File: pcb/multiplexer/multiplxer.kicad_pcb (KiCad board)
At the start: 2 copper layers, 12 parts, among them J1 Conn_01x04, U1 74HC595, U2 4051

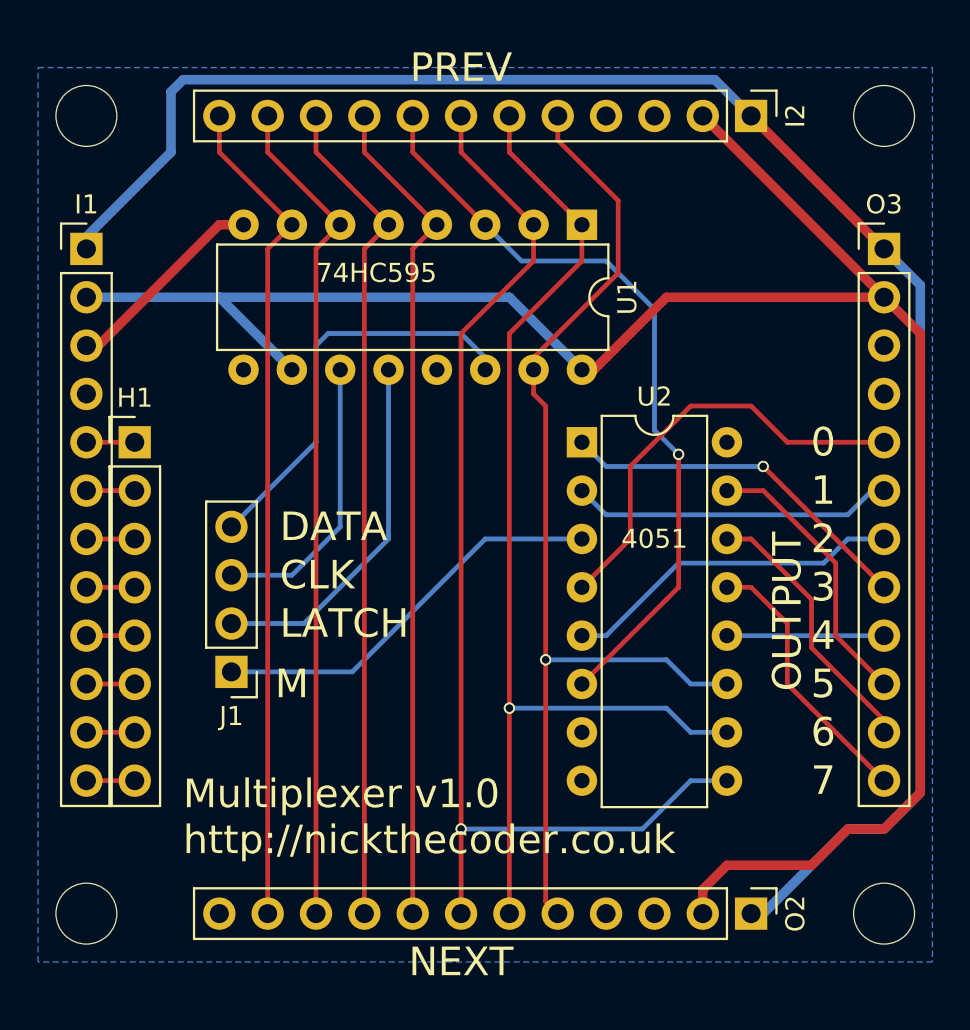
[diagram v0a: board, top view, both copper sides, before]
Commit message: Added terminal connectors to the header pins half module. Tweaked the MAX7219 module, and added both common anode and common cathode to stripLED modules.
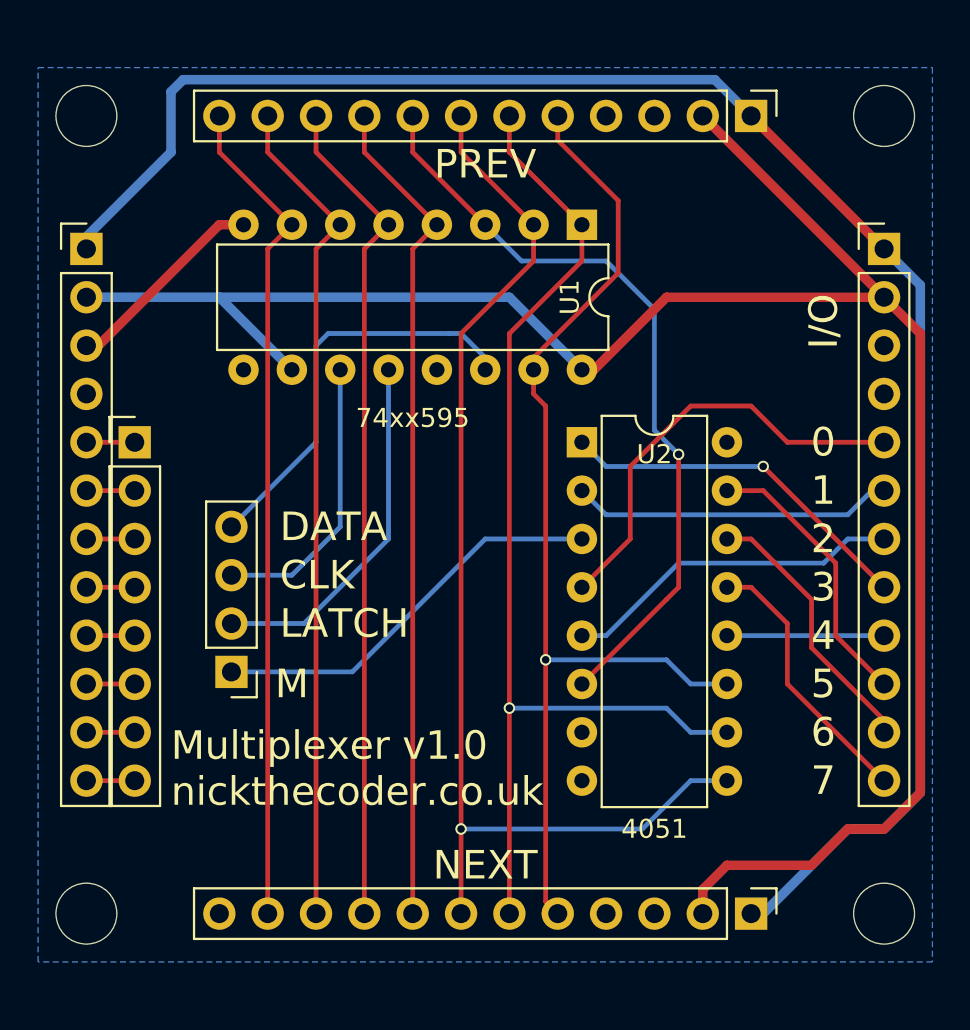
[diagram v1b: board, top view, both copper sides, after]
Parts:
- U1: value 74HC595 -> 74xx595
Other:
- board text added: "I/O"
- board text added: "Multiplexer v1.0 nickthecoder.co.uk"
- board text removed: "Multiplexer v1.0 http://nickthecoder.co.uk"
- board text removed: "OUTPUT"
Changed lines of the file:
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@@
     (links 52)
     (no_connects 0)
-    (area 124.46 82.55 173.990001 132.16)
+    (area 124.46 82.55 173.990001 132.080001)
     (thickness 1.6)
     (drawings 16)
@@
     (descr "Through hole straight pin header, 1x12, 2.54mm pitch, single row")
     (tags "Through hole pin header THT 1x12 2.54mm single row")
-    (fp_text reference I1 (at 0 -2.33) (layer F.SilkS)
+    (fp_text reference I1 (at 0 -2.33) (layer F.Fab)
       (effects (font (size 1 1) (thickness 0.15)))
     )
@@
     (descr "Through hole straight pin header, 1x08, 2.54mm pitch, single row")
     (tags "Through hole pin header THT 1x08 2.54mm single row")
-    (fp_text reference H1 (at 0 -2.33) (layer F.SilkS)
+    (fp_text reference H1 (at 0 -2.33) (layer F.Fab)
       (effects (font (size 1 1) (thickness 0.15)))
     )
@@
     (descr "Through hole straight pin header, 1x12, 2.54mm pitch, single row")
     (tags "Through hole pin header THT 1x12 2.54mm single row")
-    (fp_text reference I2 (at 0 -2.33 270) (layer F.SilkS)
+    (fp_text reference I2 (at 0 -2.33 270) (layer F.Fab)
       (effects (font (size 1 1) (thickness 0.15)))
     )
@@
     (descr "Through hole straight socket strip, 1x12, 2.54mm pitch, single row")
     (tags "Through hole socket strip THT 1x12 2.54mm single row")
-    (fp_text reference O2 (at 0 -2.33 270) (layer F.SilkS)
+    (fp_text reference O2 (at 0 -2.33 270) (layer F.Fab)
       (effects (font (size 1 1) (thickness 0.15)))
     )
@@
     (fp_line (start 1.8 29.75) (end 1.8 -1.8) (layer F.CrtYd) (width 0.05))
     (fp_line (start 1.8 -1.8) (end -1.8 -1.8) (layer F.CrtYd) (width 0.05))
-    (fp_text user %R (at 0 -2.33 270) (layer F.Fab)
+    (fp_text user %R (at 0 -2.33 270) (layer F.Fab) hide
       (effects (font (size 1 1) (thickness 0.15)))
     )
@@
     (descr "Through hole straight socket strip, 1x12, 2.54mm pitch, single row")
     (tags "Through hole socket strip THT 1x12 2.54mm single row")
-    (fp_text reference O3 (at 0 -2.33) (layer F.SilkS)
+    (fp_text reference O3 (at 0 -2.33) (layer F.Fab)
       (effects (font (size 1 1) (thickness 0.15)))
     )
@@
     (fp_line (start 1.8 29.75) (end 1.8 -1.8) (layer F.CrtYd) (width 0.05))
     (fp_line (start 1.8 -1.8) (end -1.8 -1.8) (layer F.CrtYd) (width 0.05))
-    (fp_text user %R (at 0 -2.33) (layer F.Fab)
+    (fp_text user %R (at 0 -2.33) (layer F.Fab) hide
       (effects (font (size 1 1) (thickness 0.15)))
     )
@@
     (descr "16-lead dip package, row spacing 7.62 mm (300 mils)")
     (tags "DIL DIP PDIP 2.54mm 7.62mm 300mil")
-    (fp_text reference U1 (at 3.81 -2.39 270) (layer F.SilkS)
-      (effects (font (size 1 1) (thickness 0.15)))
-    )
-    (fp_text value 74HC595 (at 2.54 10.795 360) (layer F.SilkS)
+    (fp_text reference U1 (at 3.81 0.635 270) (layer F.SilkS)
+      (effects (font (size 1 1) (thickness 0.15)))
+    )
+    (fp_text value 74xx595 (at 10.16 8.89 360) (layer F.SilkS)
       (effects (font (size 1 1) (thickness 0.15)))
     )
@@
     (descr "16-lead dip package, row spacing 7.62 mm (300 mils)")
     (tags "DIL DIP PDIP 2.54mm 7.62mm 300mil")
-    (fp_text reference U2 (at 3.81 -2.39) (layer F.SilkS)
-      (effects (font (size 1 1) (thickness 0.15)))
-    )
-    (fp_text value 4051 (at 3.81 5.08) (layer F.SilkS)
+    (fp_text reference U2 (at 3.81 0.635) (layer F.SilkS)
+      (effects (font (size 1 1) (thickness 0.15)))
+    )
+    (fp_text value 4051 (at 3.81 20.32) (layer F.SilkS)
       (effects (font (size 1 1) (thickness 0.15)))
     )
@@
     (descr "Through hole straight pin header, 1x04, 2.54mm pitch, single row")
     (tags "Through hole pin header THT 1x04 2.54mm single row")
-    (fp_text reference J1 (at 0 -2.33 180) (layer F.SilkS)
+    (fp_text reference J1 (at 0 -2.33 180) (layer F.Fab)
       (effects (font (size 1 1) (thickness 0.15)))
     )
@@
     (effects (font (size 1.5 1.5) (thickness 0.3)) (justify right))
   )
-  (gr_text PREV (at 147.955 83.82) (layer F.SilkS)
+  (gr_text PREV (at 149.225 88.9) (layer F.SilkS)
     (effects (font (size 1.5 1.5) (thickness 0.3)))
   )
-  (gr_text NEXT (at 147.955 130.81) (layer F.SilkS)
+  (gr_text NEXT (at 149.225 125.73) (layer F.SilkS)
     (effects (font (size 1.5 1.5) (thickness 0.3)))
   )
-  (gr_text OUTPUT (at 165.1 112.395 90) (layer F.SilkS)
+  (gr_text I/O (at 167.005 97.155 90) (layer F.SilkS)
     (effects (font (size 1.5 1.5) (thickness 0.3)))
   )
@@
     (effects (font (size 1.5 1.5) (thickness 0.3)) (justify left))
   )
-  (gr_text "Multiplexer v1.0\nhttp://nickthecoder.co.uk" (at 133.35 123.19) (layer F.SilkS)
+  (gr_text "Multiplexer v1.0\nnickthecoder.co.uk" (at 132.715 120.65) (layer F.SilkS)
     (effects (font (size 1.5 1.5) (thickness 0.3)) (justify left))
   )

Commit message: Added README.md for each of the modules, plus a few minor tweaks to PCB layouts while writing the text.
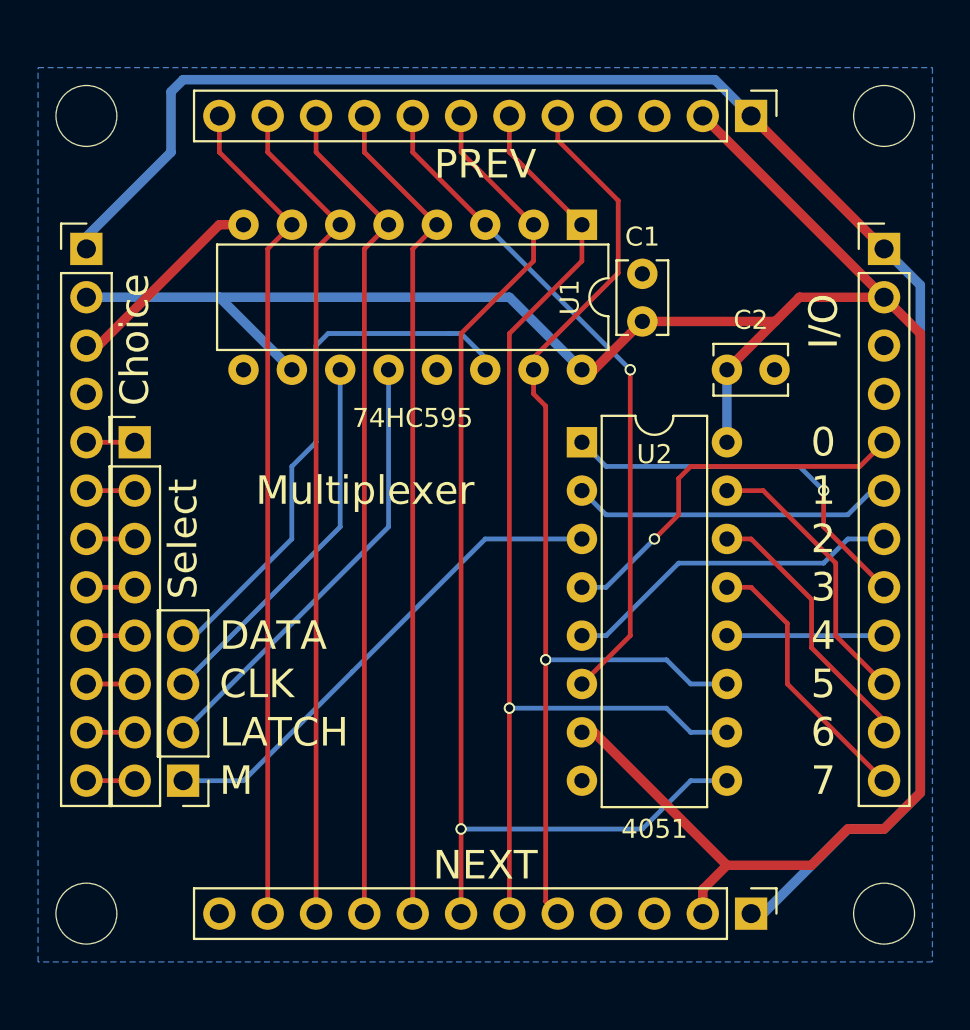
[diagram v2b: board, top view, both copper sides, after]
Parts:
- added C1: 100nF, Capacitors_THT:C_Disc_D3.8mm_W2.6mm_P2.50mm, F.Cu at (157.5, 97.2)
- added C2: 100nF, Capacitors_THT:C_Disc_D3.8mm_W2.6mm_P2.50mm, F.Cu at (161.9, 99.7)
- U1: value 74xx595 -> 74HC595
- moved J1 6.25 mm to (133.3, 121.3)
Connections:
- U2 pad 16: (no net) -> VCC
- U2 pad 7: (no net) -> VCC
- U2 pad 8: (no net) -> Earth
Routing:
- net VCC: track 105.6 -> 123.5 mm
- net /DATA: track 21.7 -> 28.8 mm
- net /CLK: track 15.0 -> 19.9 mm
- net /M: track 21.3 -> 26.2 mm
- net Net-(I2-Pad8): track 40.3 -> 35.6 mm
- net /LATCH: track 19.0 -> 23.5 mm
- net Net-(O3-Pad5): track 22.8 -> 20.1 mm, vias 0 -> 1
- net Net-(O3-Pad8): track 19.0 -> 20.1 mm
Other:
- board text added: "Choice"
- board text added: "Multiplexer"
- board text added: "Multiplexer v1.1 nickthecoder.co.uk"
- board text added: "Select"
- board text removed: "Multiplexer v1.0 nickthecoder.co.uk"
